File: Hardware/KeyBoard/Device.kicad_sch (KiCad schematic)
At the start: 0 parts

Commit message: complete layout
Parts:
- added C14, C16, C18, C20: 10uF, persional_library:C0402, symbol persional_library:0402C
- added C15, C17, C19: 100nF, persional_library:C0402, symbol persional_library:0402C
- added D1: ~, persional_library:SOD-523_L1.2-W0.8-LS1.6-FD, symbol persional_library:B5819WS_C511873
- added FPC2, FPC4: ~, persional_library:FPC-SMD_P0.50-8P_FGS-XJ-H2.0, symbol persional_library:FPC-8Pin
- added Q1: ~, persional_library:POWERTDFN-8_L3.1-W3.1-P0.65-LS3.3-BL, symbol persional_library:EMB12P03V
- added Q2: ~, persional_library:SOT-23-3_L2.9-W1.3-P1.90-LS2.4-BR, symbol persional_library:S8050_C2926165
- added R30, R31: 5.1kΩ, persional_library:R0402, symbol persional_library:0402R
- added R32, R36: 100kΩ, persional_library:R0402, symbol persional_library:0402R
- added R33: 4.7Ω, persional_library:R0402, symbol persional_library:0402R
- added R34, R35: 10kΩ, persional_library:R0402, symbol persional_library:0402R
- added R37: 1kΩ, persional_library:R0402, symbol persional_library:0402R
- added U15: ~, persional_library:SOP-16, symbol persional_library:HS8836A
- added U16: ~, persional_library:CONN-SMD_2P-P2.50_HCTL_HC-XH-2ALT, symbol persional_library:ZX-XH2.54-2PLT
- added U17: ~, persional_library:ESOP-8_L4.9-W3.9-P1.27-LS6.0-BL-EP, symbol persional_library:TP4056_C382139
- added USBC1: ~, persional_library:USB-C-SMD_TYPE-C-USB-17, symbol persional_library:USB3.1C16PFSMT
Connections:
- new net: Q2.1 (B), R34.2, R35.1
- new net: Q1.4 (G), Q2.3 (C), R36.2
- new net: R31.2, USBC1.A5 (CC1)
- new net: R30.2, USBC1.B5 (CC2)
- new net: C14.1, C15.2, U15.12 (DCP), U15.14 (V33)
- new net: C16.1, R33.1, U15.13 (VCC)
- new net: R32.1, U15.9 (REXT)
- new net: D1.2 (K), Q1.1 (S), Q1.2 (S), Q1.3 (S), R36.1, U16.1
- new net: R37.2, U17.2 (PROG)
- new net +5V: C19.2, C20.1, FPC2.7, FPC2.8, FPC4.7, FPC4.8, Q1.5 (D), Q1.6 (D), Q1.7 (D), Q1.8 (D), U17.5 (BAT)
- new net GND: C14.2, C15.1, C16.2, C17.1, C18.2, C19.1, C20.2, D1.1 (A), FPC2.10, FPC2.5, FPC2.6, FPC2.9, FPC4.10, FPC4.5, FPC4.6, FPC4.9, Q2.2 (E), R30.1, R31.1, R32.2, R33.2, R35.2, R37.1, U15.16 (GND), U16.2, U16.3, U16.4, U17.1 (TEMP), U17.3 (GND), U17.9 (EP), USBC1.0, USBC1.A1 (GND), USBC1.A12 (GND)
- new net UART_RX: FPC2.4
- new net UART_TX: FPC2.3
- new net USB_DM_1: U15.1 (OUT_D-4)
- new net USB_DM_2: FPC2.1, U15.3 (OUT_D-3)
- new net USB_DM_3: FPC4.1, U15.5 (OUT_D-2)
- new net USB_DM_4: FPC4.3, U15.7 (OUT_D-1)
- new net USB_DM_HUB: U15.10 (IN_D-), USBC1.A7 (DN1), USBC1.B7 (DN2)
- new net USB_DP_1: U15.2 (OUT_D+4)
- new net USB_DP_2: FPC2.2, U15.4 (OUT_D+3)
- new net USB_DP_3: FPC4.2, U15.6 (OUT_D+2)
- new net USB_DP_4: FPC4.4, U15.8 (OUT_D+1)
- new net USB_DP_HUB: U15.11 (IN_D+), USBC1.A6 (DP1), USBC1.B6 (DP2)
- new net VBUS: C17.2, C18.1, R34.1, U17.4 (VCC), U17.8 (CE), USBC1.A4 (VBUS), USBC1.A9 (VBUS)
- no-connect marks 0 -> 5

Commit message: Update the PCB layout
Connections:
- net USB_DM_1 renamed USB_DN
- net USB_DM_2 renamed USB_2_DN
- net USB_DM_3 renamed USB_3_DN
- net USB_DM_4 renamed USB_4_DN
- net USB_DM_HUB renamed USB_HUB_DN
- net USB_DP_1 renamed USB_DP
- net USB_DP_2 renamed USB_2_DP
- net USB_DP_3 renamed USB_3_DP
- net USB_DP_4 renamed USB_4_DP
- net USB_DP_HUB renamed USB_HUB_DP

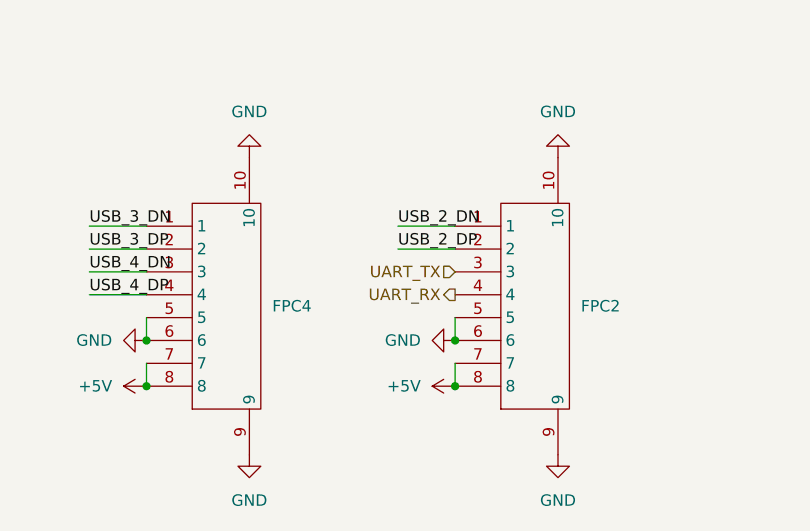
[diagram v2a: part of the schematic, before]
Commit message: Complete the non-power line routing
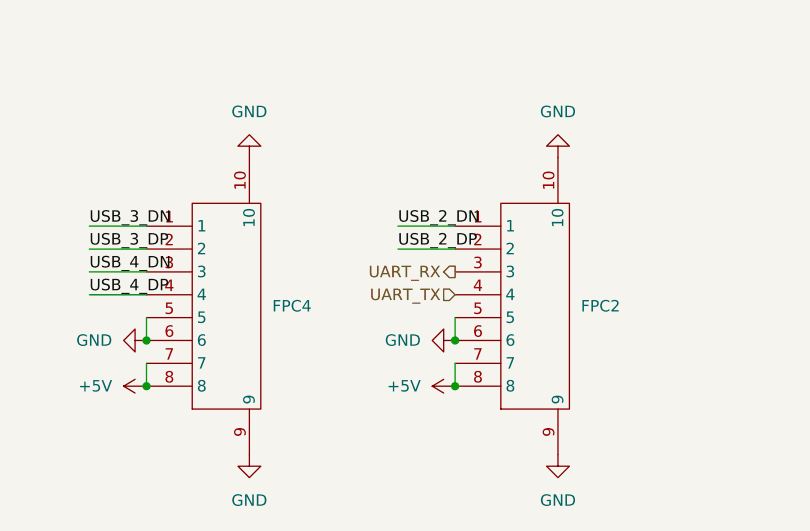
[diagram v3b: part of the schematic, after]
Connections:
- net UART_RX: now also FPC2.3; no longer FPC2.4
- net UART_TX: now also FPC2.4; no longer FPC2.3
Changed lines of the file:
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@@
 		)
 	)
-	(hierarchical_label "UART_TX"
-		(shape input)
-		(at 107.95 116.84 180)
+	(hierarchical_label "USB_DP"
+		(shape bidirectional)
+		(at 99.06 29.21 180)
 		(effects
 			(font
@@
 		)
 	)
-	(hierarchical_label "USB_DP"
-		(shape bidirectional)
-		(at 99.06 29.21 180)
+	(hierarchical_label "UART_TX"
+		(shape input)
+		(at 107.95 119.38 180)
 		(effects
 			(font
@@
 	(hierarchical_label "UART_RX"
 		(shape output)
-		(at 107.95 119.38 180)
+		(at 107.95 116.84 180)
 		(effects
 			(font

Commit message: change the keyboard
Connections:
- net GND: no longer R33.2
- net VBUS: now also R33.2
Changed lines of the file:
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@@
 	(symbol
 		(lib_id "power:GND")
-		(at 160.02 29.21 90)
-		(mirror x)
-		(unit 1)
-		(exclude_from_sim no)
-		(in_bom yes)
-		(on_board yes)
-		(dnp no)
-		(fields_autoplaced yes)
-		(property "Reference" "#PWR0136"
-			(at 166.37 29.21 0)
-			(effects
-				(font
-					(size 1.27 1.27)
-				)
-				(hide yes)
-			)
-		)
-		(property "Value" "GND"
-			(at 163.83 29.21 90)
-			(effects
-				(font
-					(size 1.27 1.27)
-				)
-				(justify right)
-			)
-		)
-		(property "Footprint" ""
-			(at 160.02 29.21 0)
-			(effects
-				(font
-					(size 1.27 1.27)
-				)
-				(hide yes)
-			)
-		)
-		(property "Datasheet" ""
-			(at 160.02 29.21 0)
-			(effects
-				(font
-					(size 1.27 1.27)
-				)
-				(hide yes)
-			)
-		)
-		(property "Description" "Power symbol creates a global label with name \"GND\" , ground"
-			(at 160.02 29.21 0)
-			(effects
-				(font
-					(size 1.27 1.27)
-				)
-				(hide yes)
-			)
-		)
-		(pin "1"
-		)
-		(instances
-			(project "KeyBoard"
-				(path "/241a990a-4472-4769-ab02-cee073c97173/c39d9c37-d812-43b2-94b9-ccc1b0cc2982"
-					(reference "#PWR0136")
-					(unit 1)
-				)
-			)
-		)
-	)
-	(symbol
-		(lib_id "power:GND")
 		(at 63.5 44.45 90)
 		(mirror x)
@@
 					(unit 1)
 				)
+			)
+		)
+	)
+	(symbol
+		(lib_id "power:VBUS")
+		(at 160.02 29.21 270)
+		(unit 1)
+		(exclude_from_sim no)
+		(in_bom yes)
+		(on_board yes)
+		(dnp no)
+		(fields_autoplaced yes)
+		(property "Reference" "#PWR0136"
+			(at 156.21 29.21 0)
+			(effects
+				(font
+					(size 1.27 1.27)
+				)
+				(hide yes)
+			)
+		)
+		(property "Value" "VBUS"
+			(at 163.83 29.21 90)
+			(effects
+				(font
+					(size 1.27 1.27)
+				)
+				(justify left)
+			)
+		)
+		(property "Footprint" ""
+			(at 160.02 29.21 0)
+			(effects
+				(font
+					(size 1.27 1.27)
+				)
+				(hide yes)
+			)
+		)
+		(property "Datasheet" ""
+			(at 160.02 29.21 0)
+			(effects
+				(font
+					(size 1.27 1.27)
+				)
+				(hide yes)
+			)
+		)
+		(property "Description" "Power symbol creates a global label with name \"VBUS\""
+			(at 160.02 29.21 0)
+			(effects
+				(font
+					(size 1.27 1.27)
+				)
+				(hide yes)
+			)
+		)
+		(pin "1"
+		)
+		(instances
+			(project "KeyBoard"
+				(path "/241a990a-4472-4769-ab02-cee073c97173/c39d9c37-d812-43b2-94b9-ccc1b0cc2982"
+					(reference "#PWR0136")
+					(unit 1)
+				)

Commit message: complete desin
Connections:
- net +5V: now also D1.2 (K), Q1.1 (S), Q1.2 (S), Q1.3 (S), R36.1, U16.1
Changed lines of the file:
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@@
+	)
+	(symbol
+		(lib_id "power:+5V")
+		(at 129.54 62.23 0)
+		(unit 1)
+		(exclude_from_sim no)
+		(in_bom yes)
+		(on_board yes)
+		(dnp no)
+		(fields_autoplaced yes)
+		(property "Reference" "#PWR0277"
+			(at 129.54 66.04 0)
+			(effects
+				(font
+					(size 1.27 1.27)
+				)
+				(hide yes)
+			)
+		)
+		(property "Value" "+5V"
+			(at 129.54 57.15 0)
+			(effects
+				(font
+					(size 1.27 1.27)
+				)
+			)
+		)
+		(property "Footprint" ""
+			(at 129.54 62.23 0)
+			(effects
+				(font
+					(size 1.27 1.27)
+				)
+				(hide yes)
+			)
+		)
+		(property "Datasheet" ""
+			(at 129.54 62.23 0)
+			(effects
+				(font
+					(size 1.27 1.27)
+				)
+				(hide yes)
+			)
+		)
+		(property "Description" "Power symbol creates a global label with name \"+5V\""
+			(at 129.54 62.23 0)
+			(effects
+				(font
+					(size 1.27 1.27)
+				)
+				(hide yes)
+			)
+		)
+		(pin "1"
+		)
+		(instances
+			(project "KeyBoard"
+				(path "/241a990a-4472-4769-ab02-cee073c97173/c39d9c37-d812-43b2-94b9-ccc1b0cc2982"
+					(reference "#PWR0277")
+					(unit 1)
+				)
+			)
+		)
 	)
 	(symbol
